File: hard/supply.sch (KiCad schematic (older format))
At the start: 0 parts

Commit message: update for kaese
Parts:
- added DCDC?: TPS54302DDCR, Package_TO_SOT_SMD:SOT-23-6_Handsoldering, symbol led_matrix:TPS54302DDCR
- added L?: 8u2, led_matrix:L_Sunking_MWSA0603S, symbol led_matrix:8u2
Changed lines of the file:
@@
 $Descr A4 11693 8268
 encoding utf-8
-Sheet 1 5
+Sheet 4 5
 Title ""
 Date ""
@@
 Comment4 ""
 $EndDescr
+$Comp
+L led_matrix:8u2 L?
+U 1 1 6056783E
+P 5200 3850
+F 0 "L?" H 5252 3896 50  0000 L CNN
+F 1 "8u2" H 5252 3805 50  0000 L CNN
+F 2 "led_matrix:L_Sunking_MWSA0603S" H 5200 3850 50  0001 C CNN
+F 3 "https://datasheet.lcsc.com/szlcsc/1912111437_Sunlord-MWSA0603S-8R2MT_C408450.pdf" H 5200 3850 50  0001 C CNN
+F 4 "" H 5200 3850 50  0001 C CNN "DigiKey_Part_Number"
+F 5 "" H 5200 3850 50  0001 C CNN "Mouser_Part_Number"
+F 6 "C408450" H 5200 3850 50  0001 C CNN "JLCPCB_Part_Number"
+F 7 "Sunlord" H 5200 3850 50  0001 C CNN "MF"
+F 8 "MWSA0603S-8R2MT" H 5200 3850 50  0001 C CNN "MPN"
+F 9 "8.2UH ±20% 5A 60MΩ SMD,6.6X7.0X3.0MM POWER INDUCTORS ROHS" H 5200 3850 50  0001 C CNN "Description"
+	1    5200 3850
+	0    -1   -1   0
+$EndComp
+$Comp
+L led_matrix:TPS54302DDCR DCDC?
+U 1 1 6056940B
+P 3950 3250
+F 0 "DCDC?" H 3950 3415 50  0000 C CNN
+F 1 "TPS54302DDCR" H 3950 3324 50  0000 C CNN
+F 2 "Package_TO_SOT_SMD:SOT-23-6_Handsoldering" H 3950 3250 50  0001 C CNN
+F 3 "https://www.ti.com/lit/gpn/TPS54302" H 3950 3250 50  0001 C CNN
+F 4 "296-46237-1-ND" H 3950 3250 50  0001 C CNN "DigiKey_Part_Number"
+F 5 "C311983" H 3950 3250 50  0001 C CNN "JLCPCB_Part_Number"
+F 6 "Texas Instruments" H 3950 3250 50  0001 C CNN "MF"
+F 7 "TPS54302DDCR" H 3950 3250 50  0001 C CNN "MPN"
+F 8 "IC REG BUCK ADJ 3A TSOT23-6" H 3950 3250 50  0001 C CNN "Description"
+	1    3950 3250
+	1    0    0    -1
+$EndComp
 $EndSCHEMATC

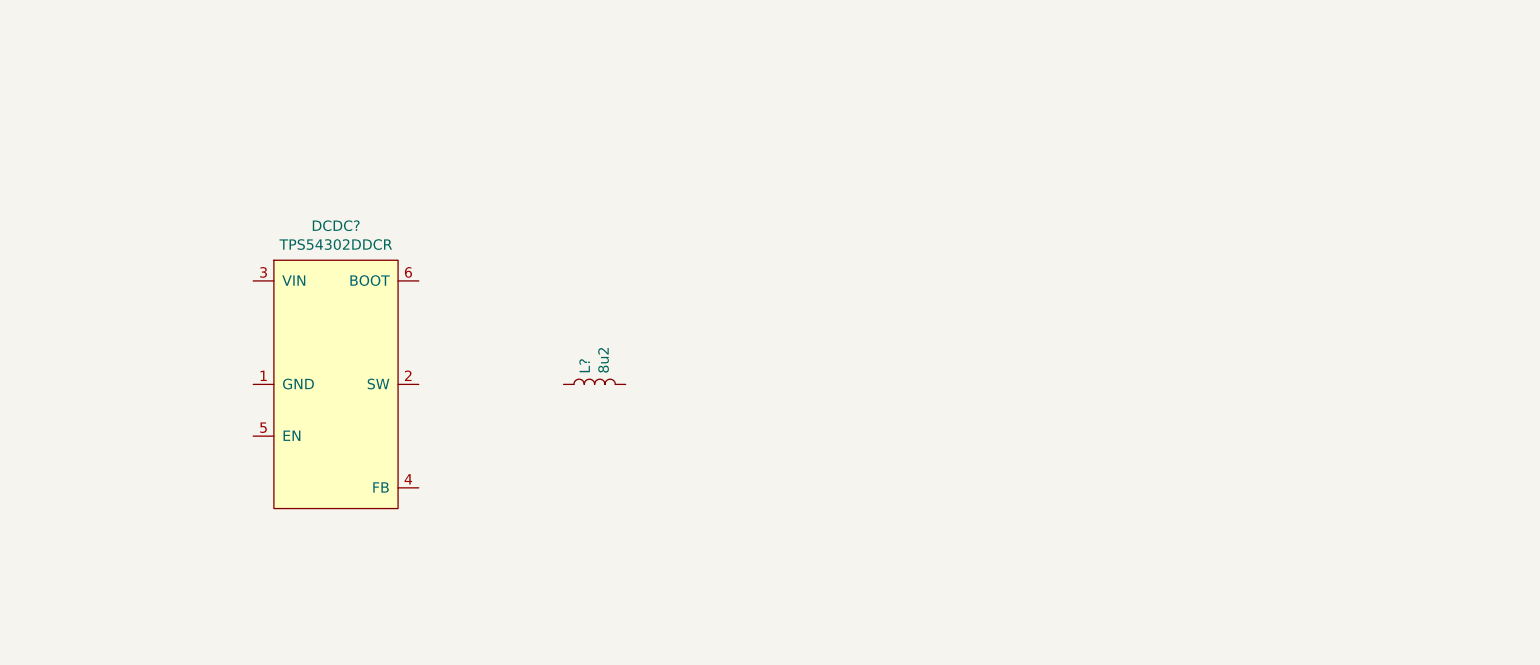
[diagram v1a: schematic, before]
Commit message: finished dc dc schematic
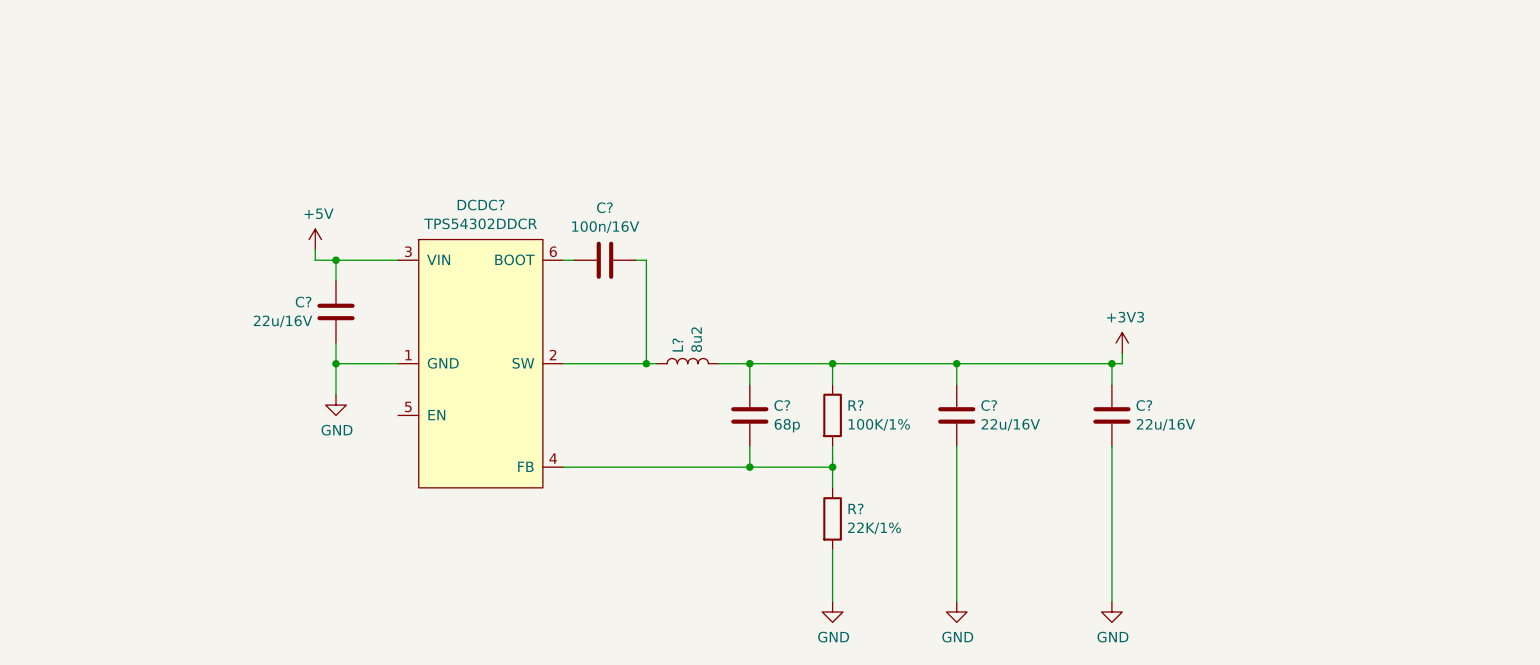
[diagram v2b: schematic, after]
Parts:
- added C? (x3): 22u/16V, Capacitor_SMD:C_0805_2012Metric, symbol Device:C
- added C?: 100n/16V, Capacitor_SMD:C_0402_1005Metric, symbol Device:C
- added C?: 68p, Capacitor_SMD:C_0402_1005Metric, symbol Device:C
- added R?: 100K/1%, Resistor_SMD:R_0402_1005Metric, symbol Device:R
- added R?: 22K/1%, Resistor_SMD:R_0402_1005Metric, symbol Device:R
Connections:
- net at L?.1: now also DCDC?.2 (SW), C?.1
- net +3V3: now reaches L?.2
- net +3V3: now also C?.2, C?.2, C?.2, R?.1
- net GND: now reaches DCDC?.1 (GND)
- net GND: now also C?.1, C?.1, C?.1, R?.2
- net +5V: now reaches DCDC?.3 (VIN)
- net +5V: now also C?.2
- net at DCDC?.4 (FB): now also C?.1, R?.1, R?.2
- net at DCDC?.6 (BOOT): now also C?.2
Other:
- moved on the sheet: DCDC?, L?

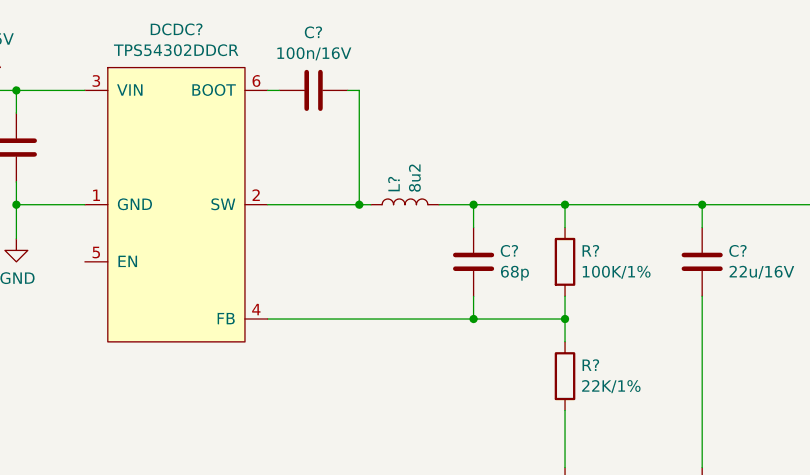
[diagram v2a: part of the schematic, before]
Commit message: added 3d model for dc dc inductor
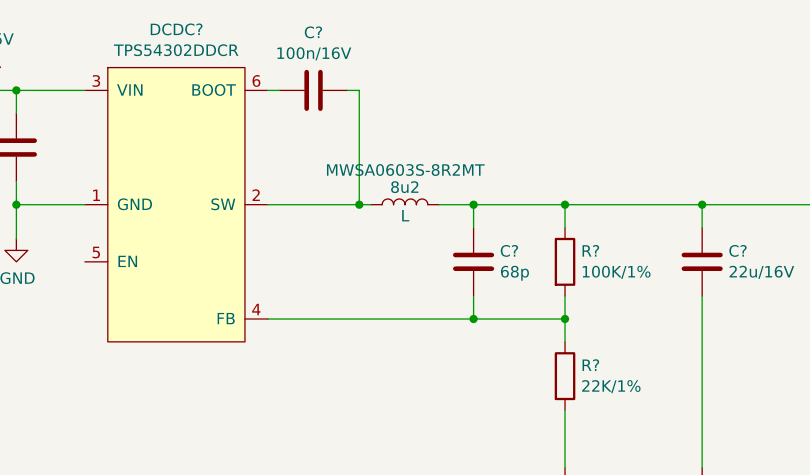
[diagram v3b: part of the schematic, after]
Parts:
- gave numbers to parts that had none: 1
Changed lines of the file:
@@
 $EndDescr
 $Comp
-L led_matrix:8u2 L?
+L led_matrix:8u2 L
 U 1 1 6056783E
 P 5650 3750
-F 0 "L?" H 5702 3796 50  0000 L CNN
-F 1 "8u2" H 5702 3705 50  0000 L CNN
+F 0 "L" V 5600 3750 50  0000 C CNN
+F 1 "8u2" V 5725 3750 50  0000 C CNN
 F 2 "led_matrix:L_Sunking_MWSA0603S" H 5650 3750 50  0001 C CNN
 F 3 "https://datasheet.lcsc.com/szlcsc/1912111437_Sunlord-MWSA0603S-8R2MT_C408450.pdf" H 5650 3750 50  0001 C CNN
@@
 F 6 "C408450" H 5650 3750 50  0001 C CNN "JLCPCB_Part_Number"
 F 7 "Sunlord" H 5650 3750 50  0001 C CNN "MF"
-F 8 "MWSA0603S-8R2MT" H 5650 3750 50  0001 C CNN "MPN"
+F 8 "MWSA0603S-8R2MT" V 5800 3750 50  0000 C CNN "MPN"
 F 9 "8.2UH ±20% 5A 60MΩ SMD,6.6X7.0X3.0MM POWER INDUCTORS ROHS" H 5650 3750 50  0001 C CNN "Description"
 	1    5650 3750

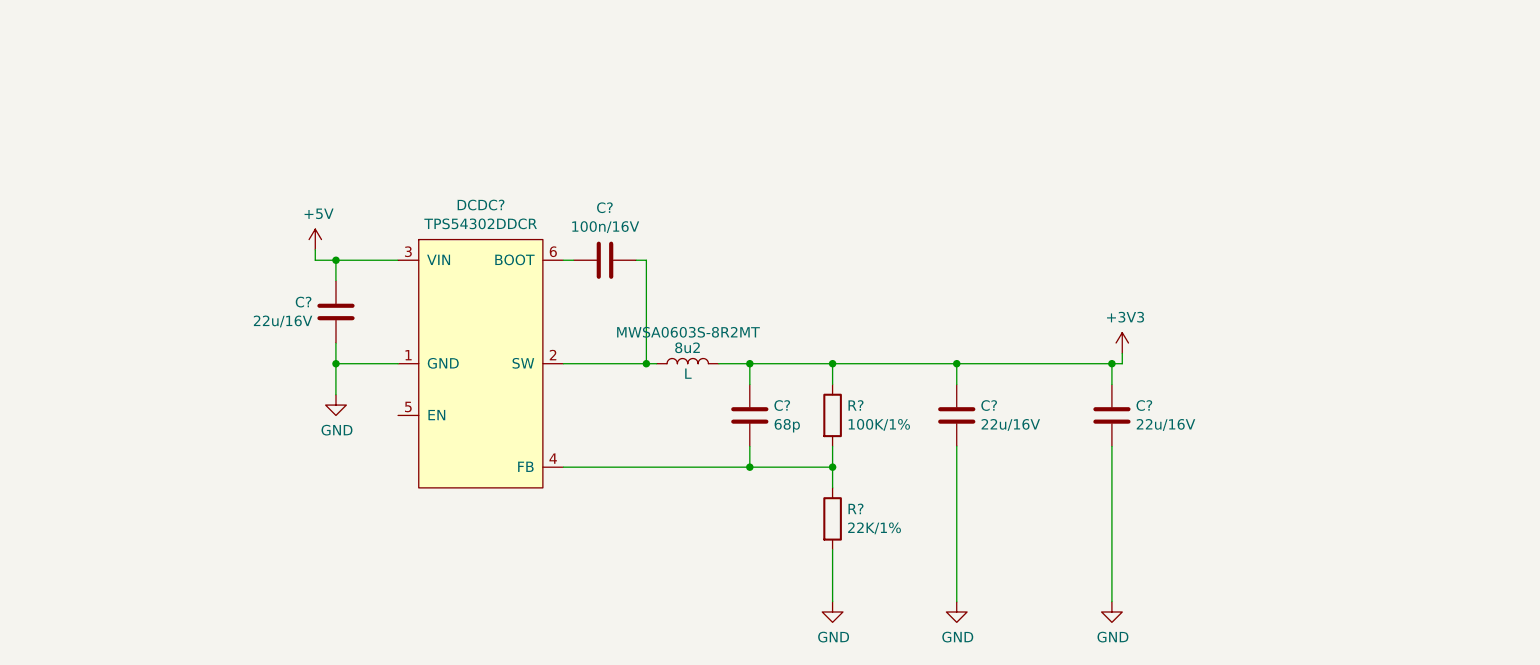
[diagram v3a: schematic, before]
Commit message: added usb connector
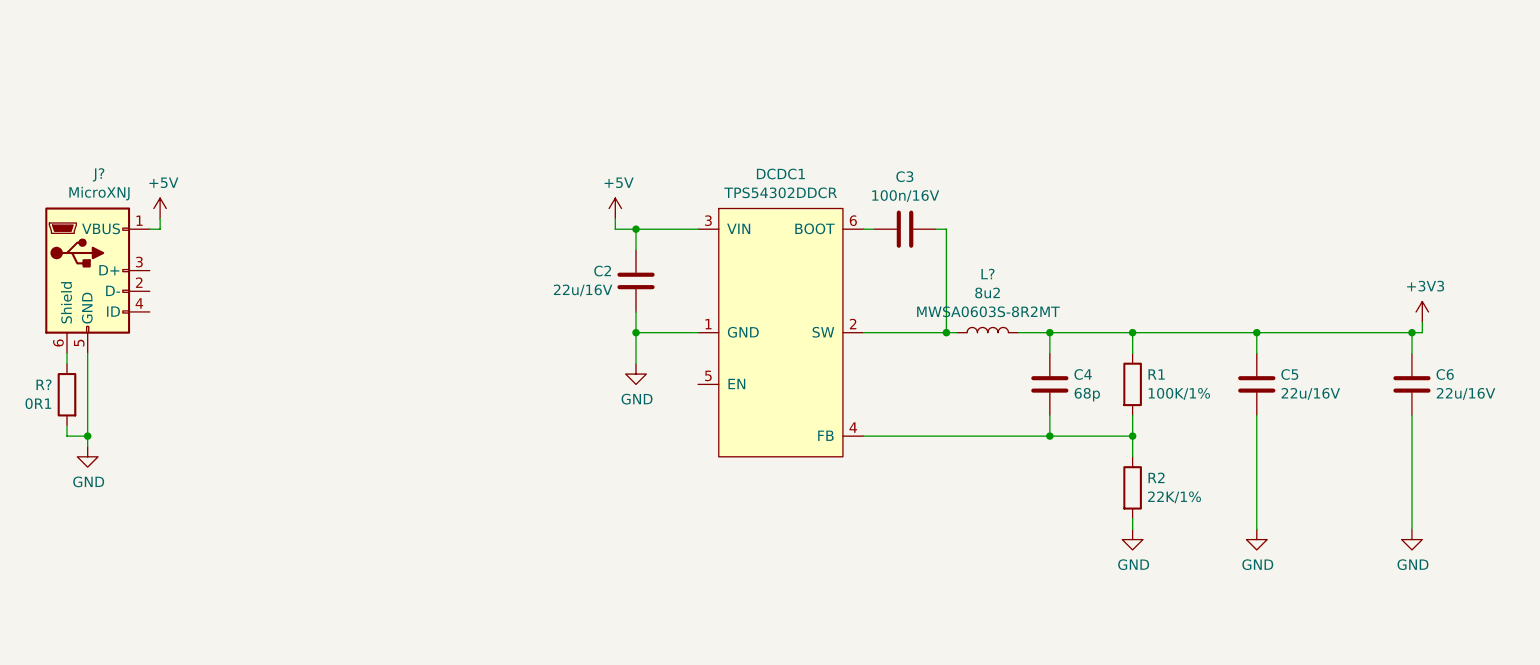
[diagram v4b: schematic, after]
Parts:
- removed L: 8u2, led_matrix:L_Sunking_MWSA0603S, symbol led_matrix:8u2
- added J?: MicroXNJ, led_matrix:Connectors_SHOU HAN_MICRO 4P DIP, symbol Connector:USB_B_Micro
- added L?: 8u2, led_matrix:L_Sunking_MWSA0603S, symbol led_matrix:8u2
- added R?: 0R1, Resistor_SMD:R_0805_2012Metric, symbol Device:R
- gave numbers to parts that had none: 8
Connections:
- net +3V3: now also L?.2
- net +5V: now also J?.1 (VBUS)
- net GND: now also J?.5 (GND), R?.2
- net at C3.1, DCDC1.2 (SW): now also L?.1
- new net: J?.6 (Shield), R?.1
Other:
- moved on the sheet: C2, C3, C4, C5, C6, DCDC1, R1, R2

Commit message: signal nmos added
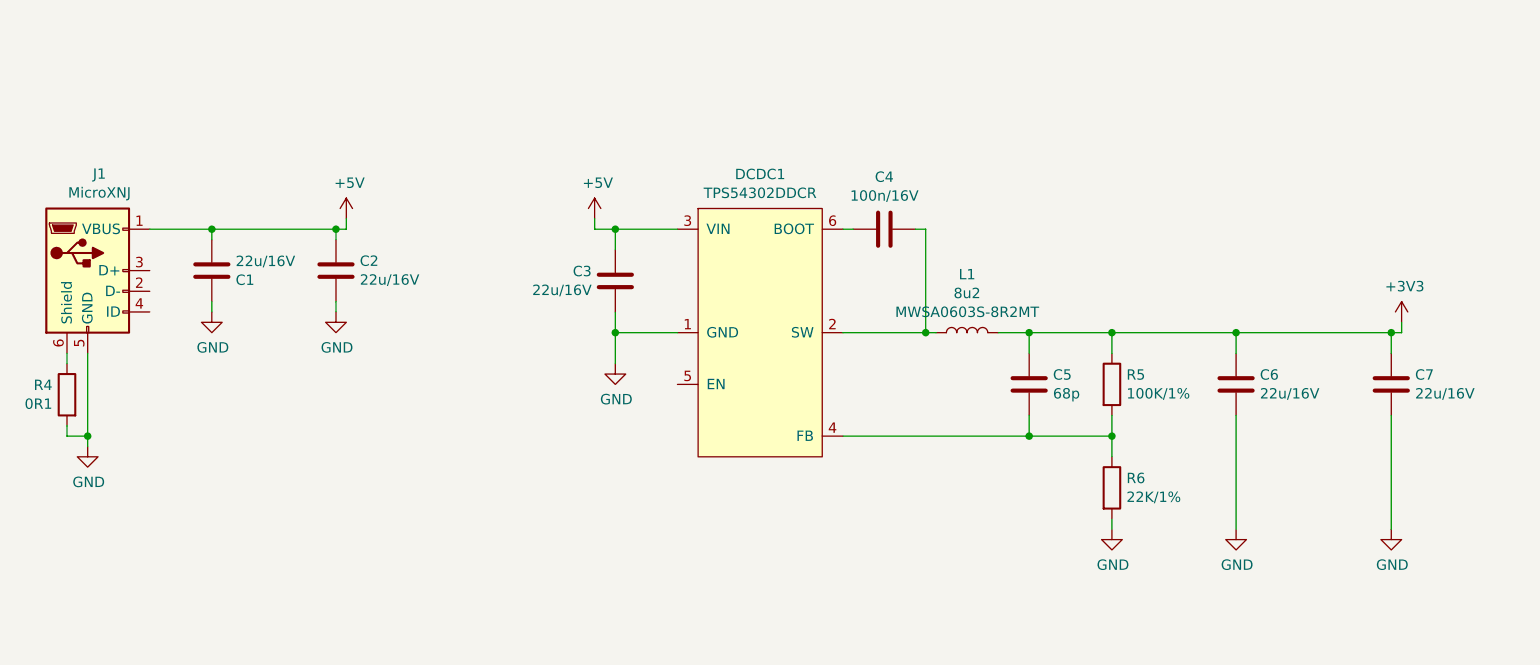
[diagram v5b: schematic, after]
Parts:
- added C1, C2: 22u/16V, Capacitor_SMD:C_0805_2012Metric, symbol Device:C
- gave numbers to parts that had none: 3
- renumbered C2 to C3, C3 to C4, C4 to C5, C5 to C6, C6 to C7, R1 to R5, R2 to R6
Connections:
- net +5V: now also C1.1, C2.2
- net GND: now also C1.2, C2.1
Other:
- moved on the sheet: C3, C4, C5, C6, C7, DCDC1, L1, R5, R6
